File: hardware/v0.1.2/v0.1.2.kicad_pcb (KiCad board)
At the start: 2 copper layers, 110 x 70 mm, 31 parts

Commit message: BOM
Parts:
- added REF**: R_0805_2012Metric, Resistor_SMD:R_0805_2012Metric, F.Cu at (217.0, 139.0)
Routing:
- net (no net): track 0.00 -> 9.82 mm
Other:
- board text added: "Component"
- board text added: "Sense"
- board text added: "Shunt Resistor - 2 terminal"

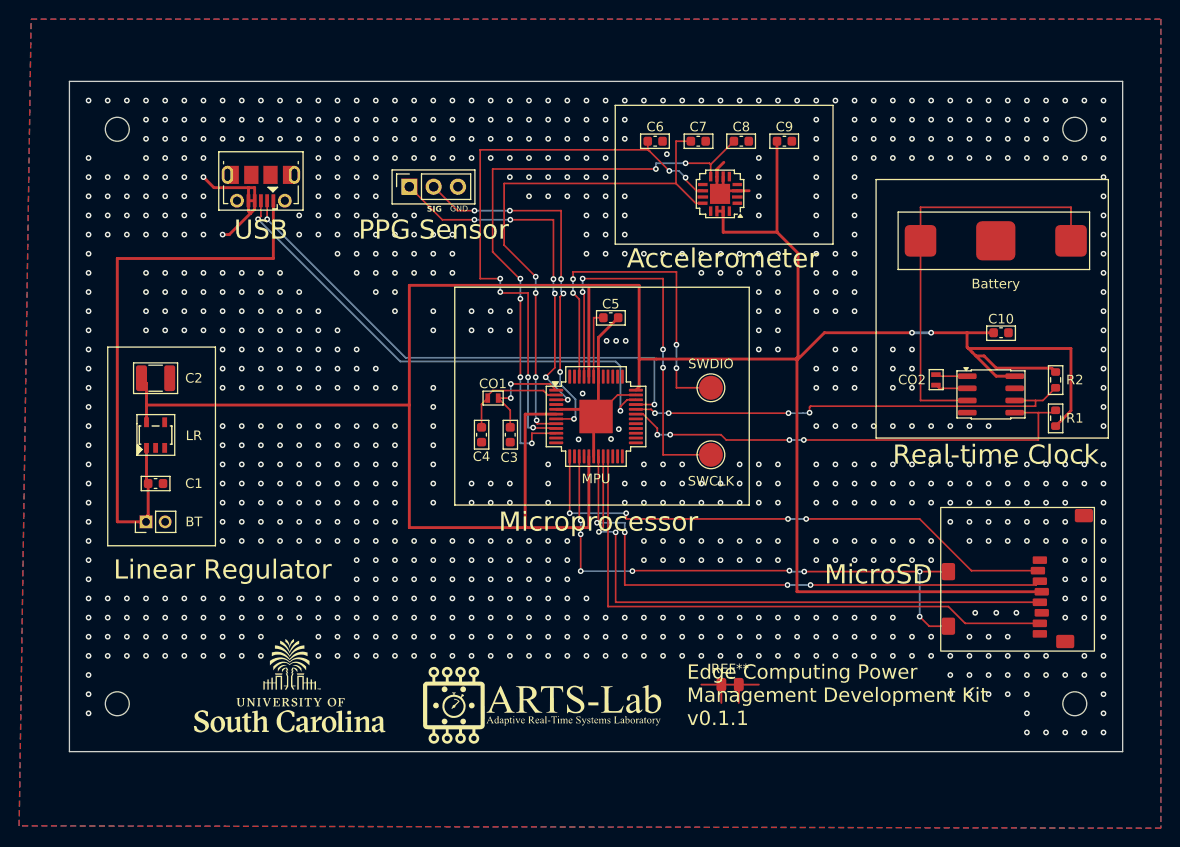
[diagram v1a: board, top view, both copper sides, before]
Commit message: moved USB on v0.1.2
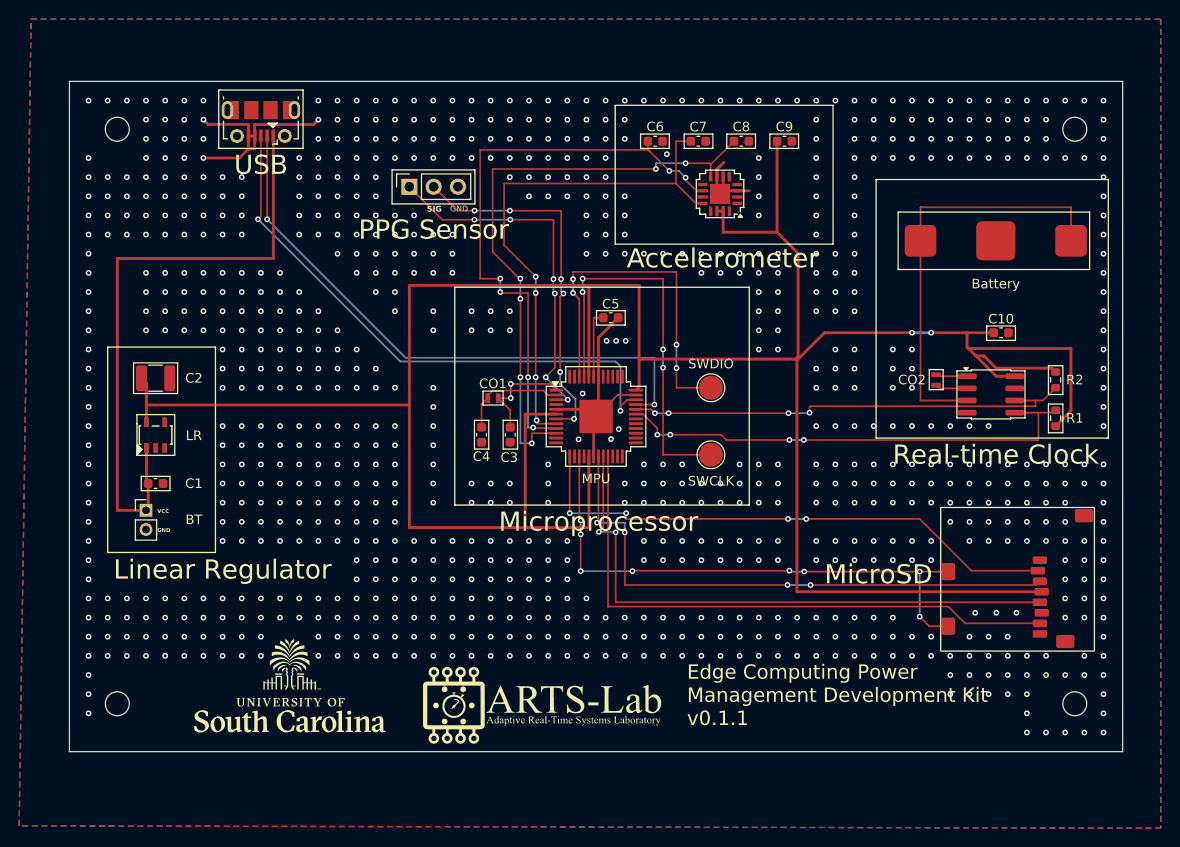
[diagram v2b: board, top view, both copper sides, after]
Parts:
- removed the REF** at (217.0, 139.0)
- moved USB 6.76 mm to (168.0, 80.2)
- moved BT 1.20 mm to (156.0, 120.8), turned to 0 degrees
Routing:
- net (no net): track 9.82 -> 0.00 mm, vias 0 -> 3
- net GND: track 48.4 -> 55.8 mm, vias 884 -> 876
- net /D-: track 55.2 -> 62.0 mm
- net /D+: track 53.4 -> 60.1 mm
- net /vUSB: track 60.7 -> 65.1 mm
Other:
- board text added: "VCC"
- board text removed: "Component"
- board text removed: "Sense"
- board text removed: "Shunt Resistor - 2 terminal"
